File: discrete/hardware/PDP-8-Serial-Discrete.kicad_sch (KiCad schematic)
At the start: 61 parts, among them J1 Screw_Terminal_01x06, J2 DE9_Socket_MountingHoles, J3 FlipChip_01x18, Q1 2N3904, Q2 2N3904, Q3 2N3906, U1 MAX232, U2 74HCT14, U3 L78L05_TO92

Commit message: Reorganised discrete hardware project
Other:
- added sheet Receiver (rx.kicad_sch)
- added sheet Transmitter (tx.kicad_sch)

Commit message: Begin multi-sheet
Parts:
- removed C10, C12, C13, C7: 100nF, Capacitor_THT:C_Disc_D5.0mm_W2.5mm_P2.50mm, symbol Device:C
- removed C11, C4, C5, C6, C9: 1uF, Capacitor_THT:C_Disc_D5.0mm_W2.5mm_P5.00mm, symbol Device:C
- removed C8: 330nF, Capacitor_THT:C_Disc_D5.0mm_W2.5mm_P5.00mm, symbol Device:C
- removed D1, D2, D3: LED, LED_THT:LED_D3.0mm, symbol Device:LED
- removed D10, D11, D4, D5, D7, D8, D9: 1N914, Diode_THT:D_DO-35_SOD27_P7.62mm_Horizontal, symbol Diode:1N914
- removed JP1: SolderJumper_2_Bridged, Jumper:SolderJumper-2_P1.3mm_Bridged2Bar_RoundedPad1.0x1.5mm, symbol Jumper:SolderJumper_2_Bridged
- removed JP2, JP3: SolderJumper_3_Bridged12, Jumper:SolderJumper-3_P1.3mm_Bridged2Bar12_RoundedPad1.0x1.5mm_NumberLabels, symbol Jumper:SolderJumper_3_Bridged12
- removed Q1, Q2: 2N3904, Package_TO_SOT_THT:TO-92_Inline, symbol Transistor_BJT:2N3904
- removed Q3: 2N3906, Package_TO_SOT_THT:TO-92_Inline, symbol Transistor_BJT:2N3906
- removed R10, R12: 330k, Resistor_THT:R_Axial_DIN0207_L6.3mm_D2.5mm_P10.16mm_Horizontal, symbol Device:R
- removed R11, R8: 100k, Resistor_THT:R_Axial_DIN0207_L6.3mm_D2.5mm_P10.16mm_Horizontal, symbol Device:R
- removed R13: 10k, Resistor_THT:R_Axial_DIN0207_L6.3mm_D2.5mm_P10.16mm_Horizontal, symbol Device:R
- removed R14, R4, R5, R6: 1k, Resistor_THT:R_Axial_DIN0207_L6.3mm_D2.5mm_P10.16mm_Horizontal, symbol Device:R
- removed R15: 3k, Resistor_THT:R_Axial_DIN0207_L6.3mm_D2.5mm_P10.16mm_Horizontal, symbol Device:R
- removed R7, R9: 47k, Resistor_THT:R_Axial_DIN0207_L6.3mm_D2.5mm_P10.16mm_Horizontal, symbol Device:R
- removed TP1: -15V, TestPoint:TestPoint_Loop_D3.50mm_Drill0.9mm_Beaded, symbol Connector:TestPoint
- removed TP2: GND, TestPoint:TestPoint_Loop_D3.50mm_Drill0.9mm_Beaded, symbol Connector:TestPoint
- removed TP6: +5V, TestPoint:TestPoint_Loop_D3.50mm_Drill0.9mm_Beaded, symbol Connector:TestPoint
- removed TP7: +10V, TestPoint:TestPoint_Loop_D3.50mm_Drill0.9mm_Beaded, symbol Connector:TestPoint
- removed U1: MAX232, Package_DIP:DIP-16_W7.62mm, symbol Interface_UART:MAX232
- removed U2: 74HCT14, Package_DIP:DIP-14_W7.62mm, symbol 74xx:74LS14
- removed U3: L78L05_TO92, Package_TO_SOT_THT:TO-92_Inline, symbol Regulator_Linear:L78L05_TO92
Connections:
- net Transmitter/DEC_TTO_232: now reaches LK1.1 (Pin_1)
- no-connect marks 14 -> 13
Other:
- sheet Receiver ports: added DEC_TTI_232, RS232_IN; removed none
- sheet Transmitter ports: added DEC_TTO_232, RS232_OUT; removed none
- note removed: "Fit either U1, U4"
- note removed: "RDR_EN"
- note removed: "TTI"
- note removed: "TTO"
- moved on the sheet: J2

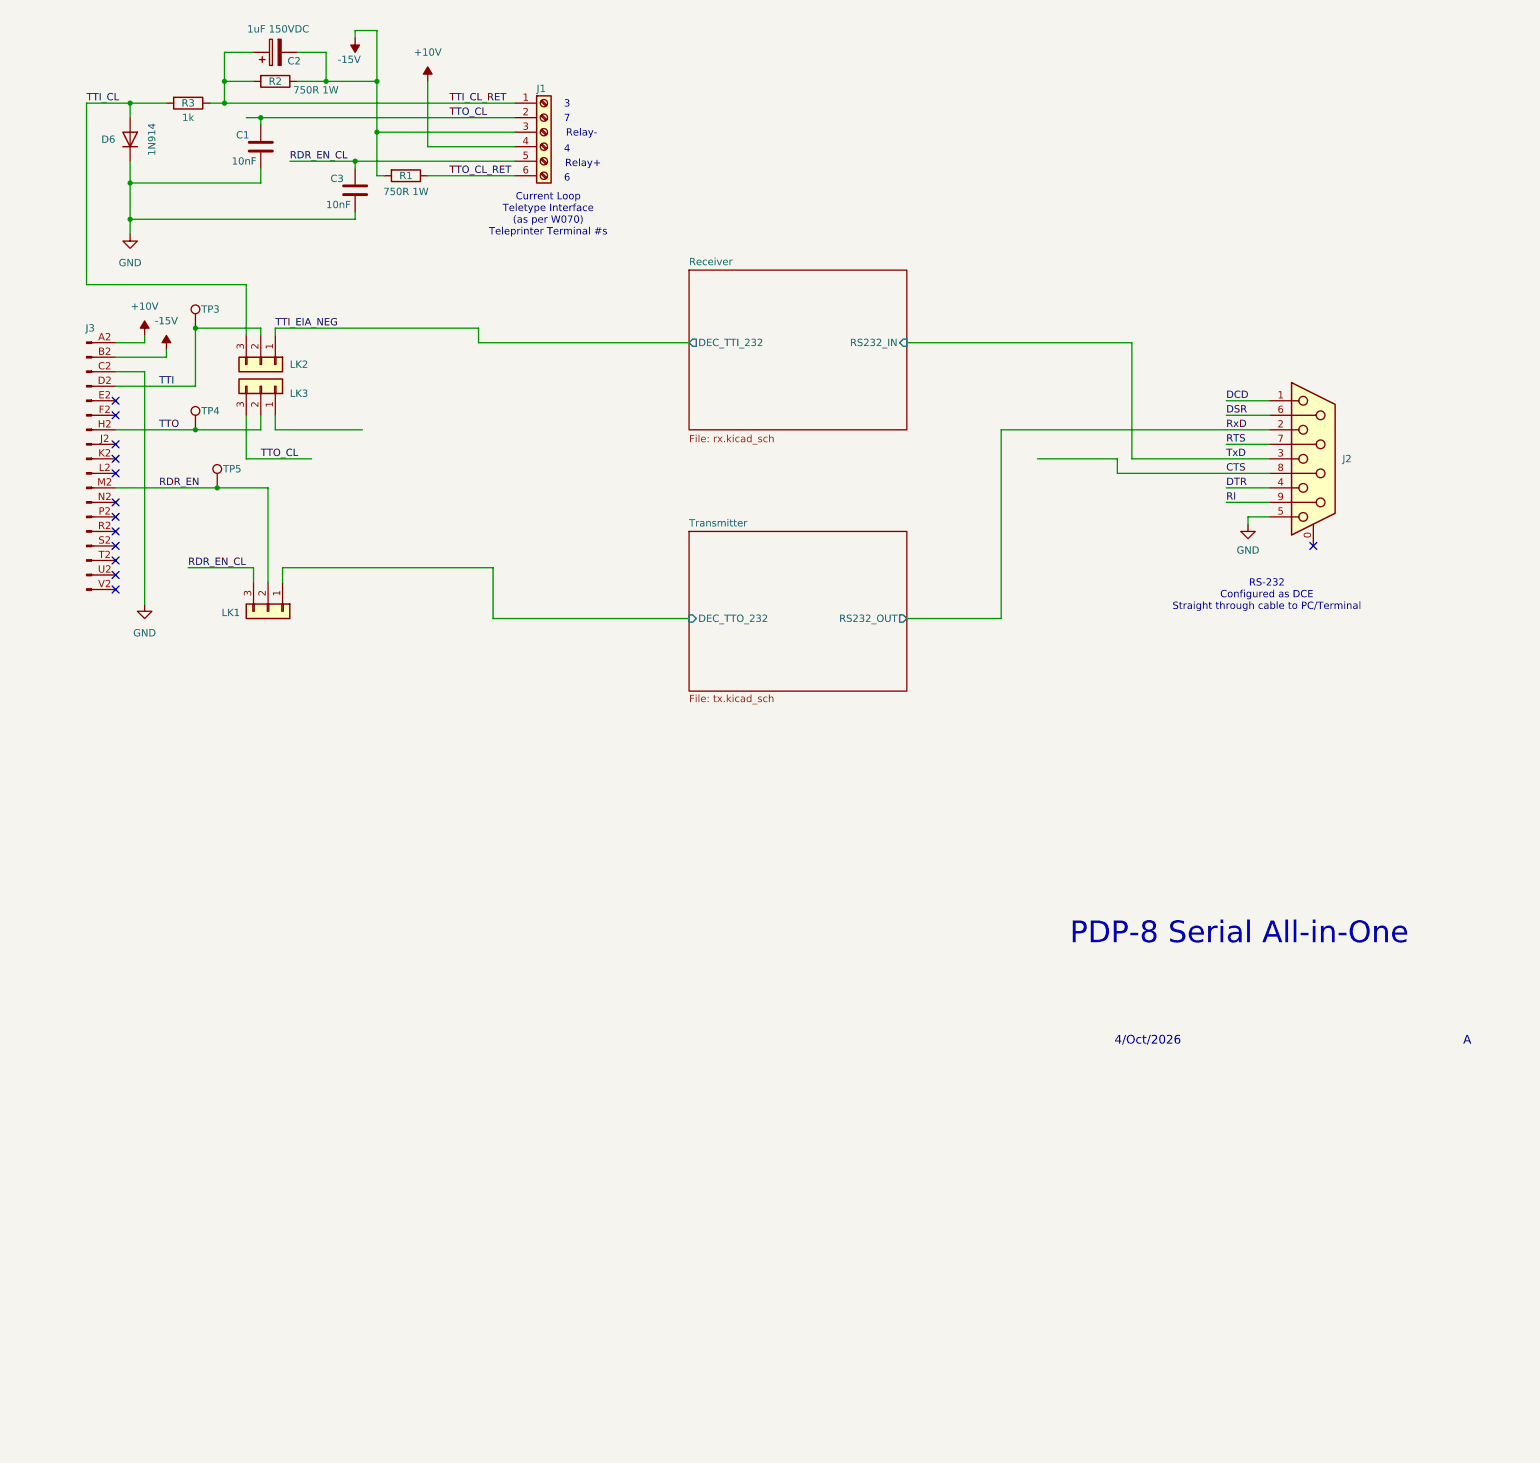
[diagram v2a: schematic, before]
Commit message: Laid out full schematic. Added decoupling and test points
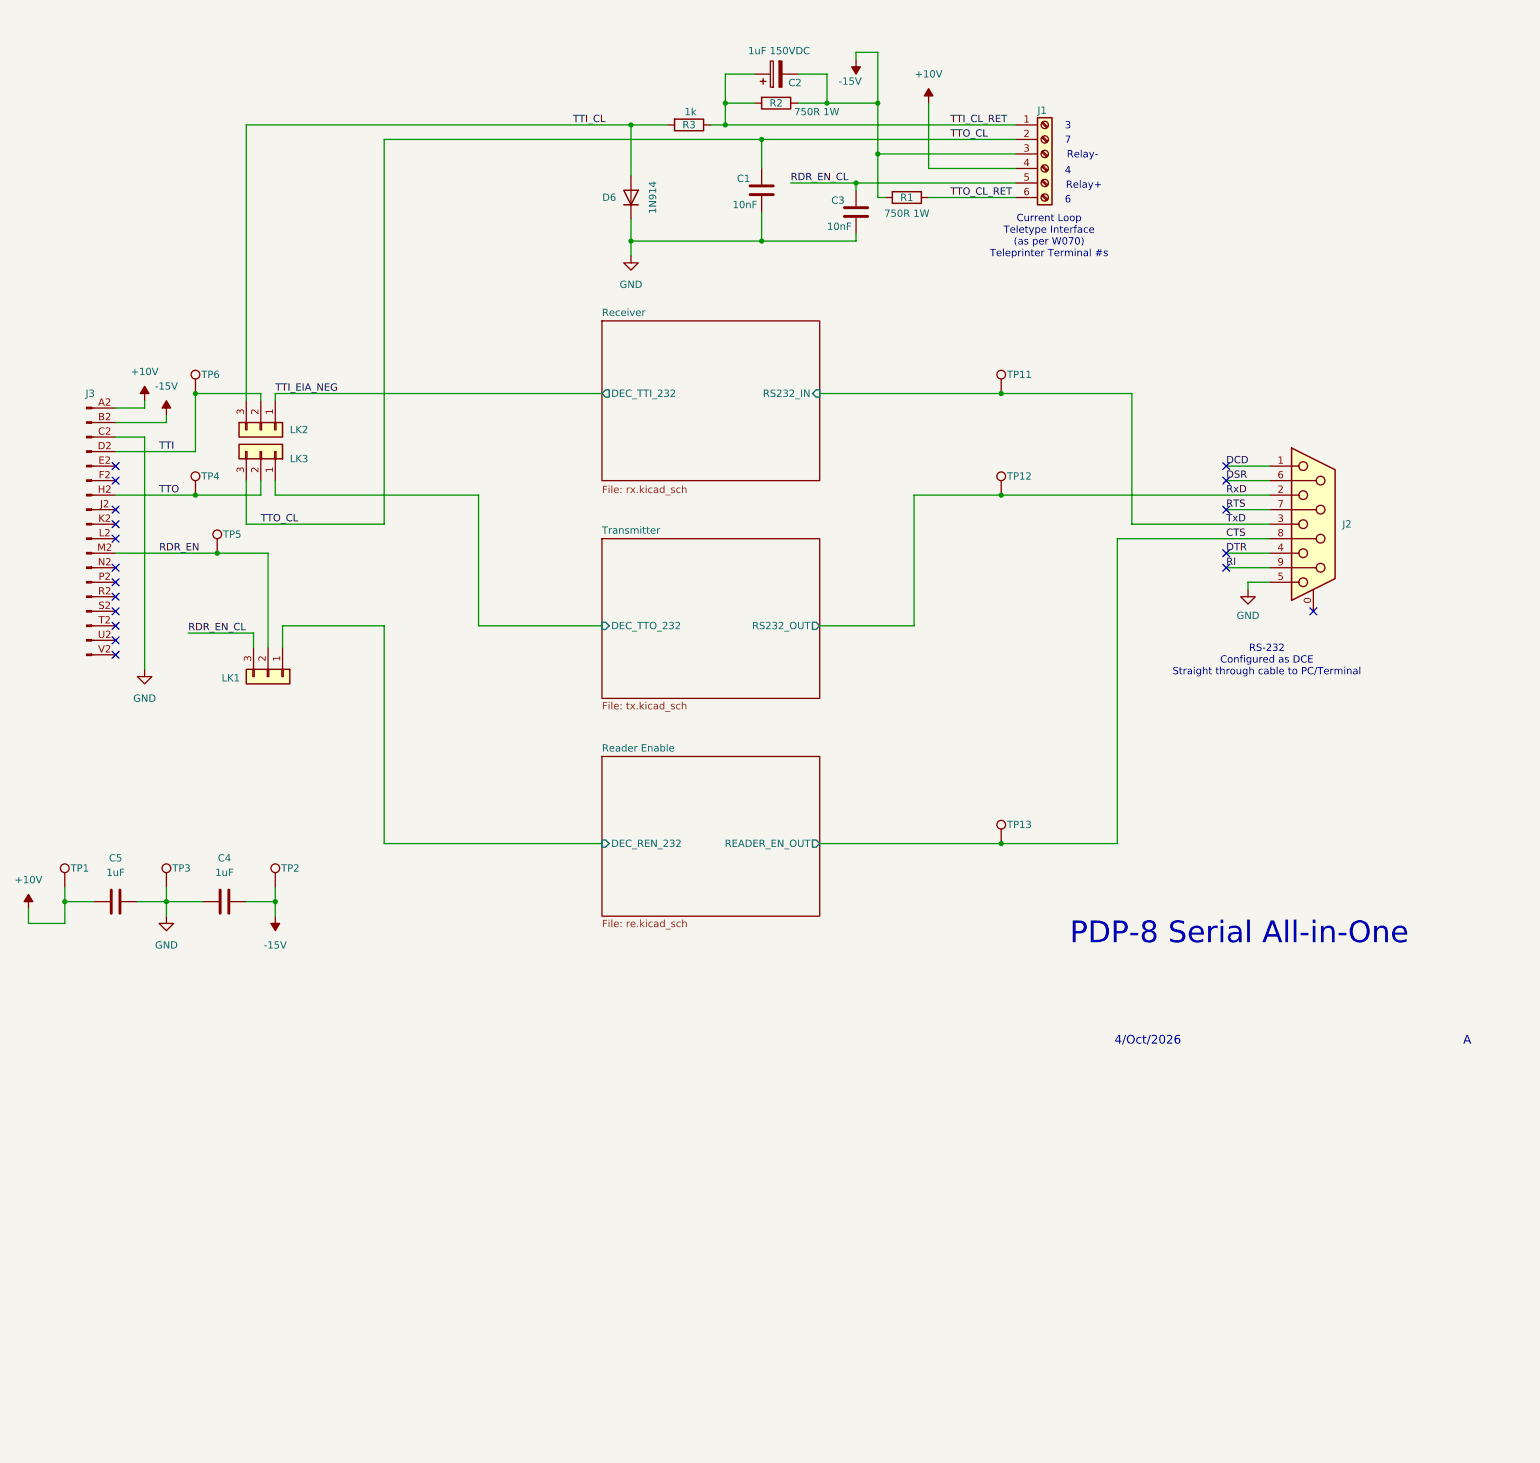
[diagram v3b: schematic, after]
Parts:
- added C4, C5: 1uF, symbol Device:C
- added TP1, TP11, TP12, TP13, TP2, TP3: TTI, TestPoint:TestPoint_Loop_D3.50mm_Drill0.9mm_Beaded, symbol Connector:TestPoint
- renumbered TP3 to TP6
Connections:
- net +10V: now also C5.1, TP1.1
- net -15V: now also C4.2, TP2.1
- net CTS: now also TP13.1
- net GND: now also C4.1, C5.2, TP3.1
- net RxD: now also TP12.1
- net Transmitter/DEC_TTO_232: now also LK3.1 (Pin_1); no longer LK1.1 (Pin_1)
- net TxD: now also TP11.1
- net DSR: now reaches J2.6
- new net Reader Enable/DEC_REN_232: LK1.1 (Pin_1)
- no-connect marks 13 -> 18
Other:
- added sheet Reader Enable (re.kicad_sch)
- moved on the sheet: C1, C2, C3, D6, J1, J2, J3, LK1, LK2, LK3, R1, R2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

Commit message: Restructured for sheet reuse of rs232 driver. Annotated functional blocks of schematic. Resolved all ERC violations
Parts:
- J3: footprint DEC:FlipChip_SingleSided_CardEdge -> Connector_PCBEdge:DEC_single_short
- renumbered C5 to C1, C4 to C2, C1 to C3, C2 to C4, C3 to C5, D6 to D1, LK2 to LK1, LK3 to LK2, LK1 to LK3, R3 to R1, R1 to R3, TP3 to TP2, TP6 to TP3, TP2 to TP6, TP11 to TP7, TP12 to TP8, TP13 to TP9
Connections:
- net Reader Enable/DEC_REN_232 renamed DEC_REN_232
- net Transmitter/DEC_TTO_232 renamed DEC_TTO_232
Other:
- removed sheet Reader Enable
- added sheet Reader Enable (CTS) (rs232_driver.kicad_sch)
- sheet Receiver: file rx.kicad_sch -> rs232_receiver.kicad_sch
- sheet Transmitter: file tx.kicad_sch -> rs232_driver.kicad_sch
- sheet Transmitter ports: added DEC_IN; removed DEC_TTO_232

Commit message: Set footprints and component ratings
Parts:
- C1, C2: footprint (none) -> Capacitor_THT:C_Disc_D5.0mm_W2.5mm_P5.00mm
- R1: footprint Resistor_THT:R_Axial_DIN0207_L6.3mm_D2.5mm_P10.16mm_Horizontal -> Resistor_THT:R_Axial_DIN0414_L11.9mm_D4.5mm_P20.32mm_Horizontal
- R2, R3: value 750R 1W -> 750R
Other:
- note added: "1W"
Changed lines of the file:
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@@
 		)
 	)
+	(text "1W"
+		(exclude_from_sim no)
+		(at 153.67 32.004 0)
+		(effects
+			(font
+				(size 1.27 1.27)
+			)
+		)
+	)
+	(text "1W"
+		(exclude_from_sim no)
+		(at 137.668 30.988 0)
+		(effects
+			(font
+				(size 1.27 1.27)
+			)
+		)
+	)
 	(text "Relay+"
 		(exclude_from_sim no)
@@
 		)
 	)
+	(text "1W"
+		(exclude_from_sim no)
+		(at 177.038 48.768 0)
+		(effects
+			(font
+				(size 1.27 1.27)
+			)
+		)
+	)
 	(text "PDP-8 Serial All-in-One"
 		(exclude_from_sim no)
@@
 			)
 		)
-		(property "Value" "750R 1W"
-			(at 158.242 30.734 90)
+		(property "Value" "750R"
+			(at 149.098 31.75 90)
 			(effects
 				(font
@@
 		)
 		(property "Value" "1k"
-			(at 136.144 30.734 90)
+			(at 134.112 30.734 90)
 			(effects
 				(font
@@
 			)
 		)
-		(property "Footprint" "Resistor_THT:R_Axial_DIN0207_L6.3mm_D2.5mm_P10.16mm_Horizontal"
+		(property "Footprint" "Resistor_THT:R_Axial_DIN0414_L11.9mm_D4.5mm_P20.32mm_Horizontal"
 			(at 135.89 31.242 90)
 			(effects
@@
 			)
 		)
-		(property "Value" "750R 1W"
-			(at 173.99 48.514 90)
+		(property "Value" "750R"
+			(at 172.466 48.514 90)
 			(effects
 				(font
@@
 			)
 		)
-		(property "Footprint" ""
+		(property "Footprint" "Capacitor_THT:C_Disc_D5.0mm_W2.5mm_P5.00mm"
 			(at 58.42 167.9448 0)
 			(effects
@@
 			)
 		)
-		(property "Footprint" ""
+		(property "Footprint" "Capacitor_THT:C_Disc_D5.0mm_W2.5mm_P5.00mm"
 			(at 39.37 167.9448 0)
 			(effects

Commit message: Added holeless flip-chip layout. Footprints assigned.
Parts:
- J3: footprint Connector_PCBEdge:DEC_single_short -> Library:DEC_single_short_holeless
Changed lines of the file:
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@@
 			)
 		)
-		(property "Footprint" "Connector_PCBEdge:DEC_single_short"
+		(property "Footprint" "Library:DEC_single_short_holeless"
 			(at 35.56 109.22 0)
 			(effects

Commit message: New footprints and symbols. PCB layout begun
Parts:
- removed LK1, LK2, LK3: Conn_01x03, Connector_PinHeader_2.54mm:PinHeader_1x03_P2.54mm_Vertical, symbol Connector_Generic:Conn_01x03
- removed TP3: TTI, TestPoint:TestPoint_Loop_D3.50mm_Drill0.9mm_Beaded, symbol Connector:TestPoint
- removed TP4: TTO, TestPoint:TestPoint_Loop_D3.50mm_Drill0.9mm_Beaded, symbol Connector:TestPoint
- removed TP5: RDR_EN, TestPoint:TestPoint_Loop_D3.50mm_Drill0.9mm_Beaded, symbol Connector:TestPoint
- added D1, D2, D3: LED, LED_THT:LED_D3.0mm, symbol Device:LED
- added LK1, LK2, LK3: Link_01x03, Connector_PinHeader_2.54mm:PinHeader_1x03_P2.54mm_Vertical, symbol Links:Link_01x03
- added R1, R3: 27k, Resistor_THT:R_Axial_DIN0207_L6.3mm_D2.5mm_P7.62mm_Horizontal, symbol Device:R
- added R2: 10k, Resistor_THT:R_Axial_DIN0207_L6.3mm_D2.5mm_P7.62mm_Horizontal, symbol Device:R
- renumbered D1 to D4, R1 to R4, R2 to R5, R3 to R6, TP6 to TP3, TP7 to TP4, TP8 to TP5, TP9 to TP6
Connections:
- net +10V: now also J3.AA2 (Pin_A); no longer J3.A2 (Pin_A)
- net -15V: now also J3.AB2 (Pin_B), D3.1 (K); no longer J3.B2 (Pin_B)
- net DEC_REN_232: now also LK3.1 (Pin_1)
- net DEC_TTO_232: now also LK2.1 (Pin_1)
- net GND: now also J3.AC2 (Pin_C), D1.2 (A), D2.2 (A); no longer J3.C2 (Pin_C)
- net RDR_EN: now also J3.AM2 (Pin_M), LK3.2 (Pin_2), R3.1; no longer J3.M2 (Pin_M)
- net RDR_EN_CL: now also LK3.3 (Pin_3)
- net TTI: now also J3.AD2 (Pin_D), LK1.2 (Pin_2), R2.1; no longer J3.D2 (Pin_D)
- net TTI_CL: now also LK1.3 (Pin_3)
- net TTI_EIA_NEG: now also LK1.1 (Pin_1)
- net TTO: now also J3.AH2 (Pin_H), LK2.2 (Pin_2), R1.1; no longer J3.H2 (Pin_H)
- net TTO_CL: now also LK2.3 (Pin_3)
- new net: D2.1 (K), R2.2
- new net: D1.1 (K), R1.2
- new net: D3.2 (A), R3.2
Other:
- moved on the sheet: C1, C2, C3, C4, C5, D4, J1, J2, R4, R5, R6, TP1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

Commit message: ERC & DRC clear. Layout complete
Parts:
- TP1: value TTI -> +10V
- TP2: value TTI -> GND
- TP3: value TTI -> -15V
- TP4: value TTI -> TxD
- TP5: value TTI -> RxD
- TP6: value TTI -> CTS
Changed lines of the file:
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@@
 	)
 	(label "TTI"
-		(at 36.83 27.94 0)
+		(at 35.56 27.94 0)
 		(effects
 			(font
@@
 	)
 	(label "TTO"
-		(at 21.59 27.94 0)
+		(at 20.32 27.94 0)
 		(effects
 			(font
@@
 			)
 		)
-		(property "Value" "TTI"
+		(property "Value" "GND"
 			(at 55.88 164.3379 0)
 			(effects
@@
 			)
 		)
-		(property "Value" "TTI"
+		(property "Value" "RxD"
 			(at 201.93 95.7579 0)
 			(effects
@@
 			)
 		)
-		(property "Value" "TTI"
+		(property "Value" "-15V"
 			(at 74.93 164.3379 0)
 			(effects
@@
 			)
 		)
-		(property "Value" "TTI"
+		(property "Value" "+10V"
 			(at 38.1 164.3379 0)
 			(effects
@@
 			)
 		)
-		(property "Value" "TTI"
+		(property "Value" "TxD"
 			(at 201.93 77.9779 0)
 			(effects
@@
 			)
 		)
-		(property "Value" "TTI"
+		(property "Value" "CTS"
 			(at 201.93 156.7179 0)
 			(effects
